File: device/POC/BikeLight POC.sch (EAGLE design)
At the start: 3 parts

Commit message: - added SD card with level shifter, FRAM module
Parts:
- added C1, C2, C3, C4, C5, C6: 0.1μF, rcl:C-EUC0805
- added IC3: FM25W256-SOIC, FM25W256 FERAM:FM25W256-SOIC
- added IC4: MICROSD_SPI_MODE, Molex SD-47309 SD Card Slot:MICROSD_SPI_MODE
- added IC5: (no value), TXB0106 - Logic Level Translator:TXB0106
- added R1, R3, R4, R5: 10k, rcl:R-EU_R0805
- added R2: 120, rcl:R-EU_R0805
- added X1, X2: 22-23-2021, con-molex:22-23-2021
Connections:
- removed net N$4: IC2.SI
- removed net N$5: IC2.SCK
- removed net N$6: IC2.!CS!
- removed net N$8: IC2.TXCAN
- removed net N$9: IC2.RXCAN
- removed net SPI_SS: U$1.D10
- new net 3V3: C4.1, C5.1, IC4.VCC, IC5.VCCA, R4.2
- new net 5V0: C1.1, C2.1, C3.1, C6.1, IC1.VCC, IC2.VDD, IC3.!HOLD!, IC3.!WP!, IC3.VCC, IC5.VCCB, R1.1, R3.2
- new net CANH: IC1.CANH, R2.2, X1-1.S
- new net CANL: IC1.CANL, R2.1, X1-2.S
- new net OE: IC5.OE, R5.2, U$1.D7
- new net RXCAN: IC1.RXD, IC2.RXCAN
- new net SD_CARD_DETECT: IC5.B6, U$1.D6
- new net SD_CARD_DETECT_3V3: IC4.CARD_DETECT, IC5.A6
- new net SPI_MISO_3V3: IC4.DO, IC5.A2
- new net SPI_MOSI_3V3: IC4.DI, IC5.A4
- new net SPI_SCK_3V3: IC4.CLK, IC5.A3
- new net SPI_SS_FRAM: IC3.!CS!, R3.1, U$1.D9
- new net SPI_SS_MCP2515: IC2.!CS!, R1.2, U$1.D10
- new net SPI_SS_SD-CARD: IC5.B5, U$1.D8
- new net SPI_SS_SD-CARD_3V3: IC4.CS, IC5.A5, R4.1
- new net STBY: IC1.STBY, U$1.D5
- new net TXCAN: IC1.TXD, IC2.TXCAN
- net GND: now also C1.2, C2.2, C3.2, C4.2, C5.2, C6.2, IC1.GND, IC2.GND, IC3.GND, IC4.GND1, IC4.GND2, IC4.GND3, IC4.GND4, IC5.GND, R5.1
- net N$3: now also IC2.OSC1; no longer IC2.SO
- net SPI_MISO: now also IC2.SO, IC3.SO, IC5.B2
- net SPI_MOSI: now also IC2.SI, IC3.SI, IC5.B4
- net SPI_SCK: now also IC2.SCK, IC3.SCK, IC5.B3
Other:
- moved on the sheet: IC1, IC2

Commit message: - added few passives to SD card, FRAM, logic level shifter, can hardware
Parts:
- added R6: 120, rcl:R-EU_R0805
- BRD1: value ARDUINOUNO -> (none)
- IC1: device MCP2561-2 - High-Speed CAN Transceiver:MCP2561-2 -> MCP2515-I-ML - Standalonce CAN Controller with SPI Interface:MCP2515-I-ML
- IC2: value (none) -> MICROSD_SPI_MODE; device MCP2515-I-ML - Standalonce CAN Controller with SPI Interface:MCP2515-I-ML -> Molex SD-47309 SD Card Slot:MICROSD_SPI_MODE
- IC4: value MICROSD_SPI_MODE -> (none); device Molex SD-47309 SD Card Slot:MICROSD_SPI_MODE -> MCP2561-2 - High-Speed CAN Transceiver:MCP2561-2
- R2: value 120 -> 10k
- renumbered U$1 to BRD1
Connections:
- net 3V3: now also C3.1, IC2.VCC, R3.2; no longer C4.1, IC4.VCC, R4.2
- net 5V0: now also C4.1, IC1.VDD, IC4.VCC, R2.2, R4.1; no longer C3.1, IC1.VCC, IC2.VDD, R3.2
- net CANH: now also IC4.CANH, R6.2, X2-1.S; no longer IC1.CANH, R2.2, X1-1.S
- net CANL: now also IC4.CANL, R6.1, X2-2.S; no longer IC1.CANL, R2.1, X1-2.S
- net GND: now also IC2.GND1, IC2.GND2, IC2.GND3, IC2.GND4, IC4.GND; no longer IC2.GND, IC4.GND1, IC4.GND2, IC4.GND3, IC4.GND4
- net N$3: now also IC1.OSC1; no longer IC2.OSC1
- net N$7: now also IC1.!INT!; no longer IC2.!INT!
- net RXCAN: now also IC1.RXCAN, IC4.RXD; no longer IC1.RXD, IC2.RXCAN
- net SD_CARD_DETECT_3V3: now also IC2.CARD_DETECT; no longer IC4.CARD_DETECT
- net SPI_MISO: now also IC1.SO; no longer IC2.SO
- net SPI_MISO_3V3: now also IC2.DO; no longer IC4.DO
- net SPI_MOSI: now also IC1.SI; no longer IC2.SI
- net SPI_MOSI_3V3: now also IC2.DI; no longer IC4.DI
- net SPI_SCK: now also IC1.SCK; no longer IC2.SCK
- net SPI_SCK_3V3: now also IC2.CLK; no longer IC4.CLK
- net SPI_SS_FRAM: now also R2.1; no longer R3.1
- net SPI_SS_MCP2515: now also IC1.!CS!; no longer IC2.!CS!
- net SPI_SS_SD-CARD_3V3: now also IC2.CS, R3.1; no longer IC4.CS, R4.1
- net STBY: now also IC4.STBY, R4.2; no longer IC1.STBY
- net TXCAN: now also IC1.TXCAN, IC4.TXD; no longer IC1.TXD, IC2.TXCAN
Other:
- moved on the sheet: C2, C3, C4, R2, R3, R4, X1-1, X1-2, X2-1, X2-2

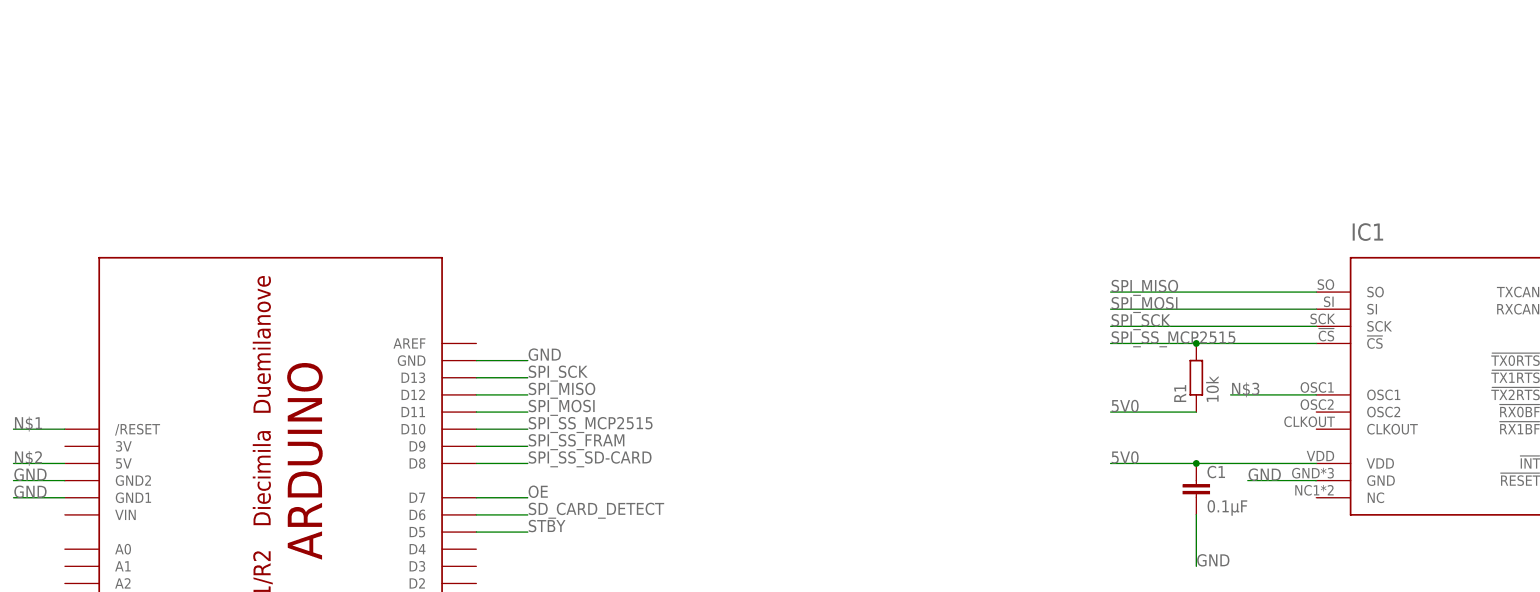
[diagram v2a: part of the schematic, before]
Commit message: - added 8mhz oscillator to mcp2515
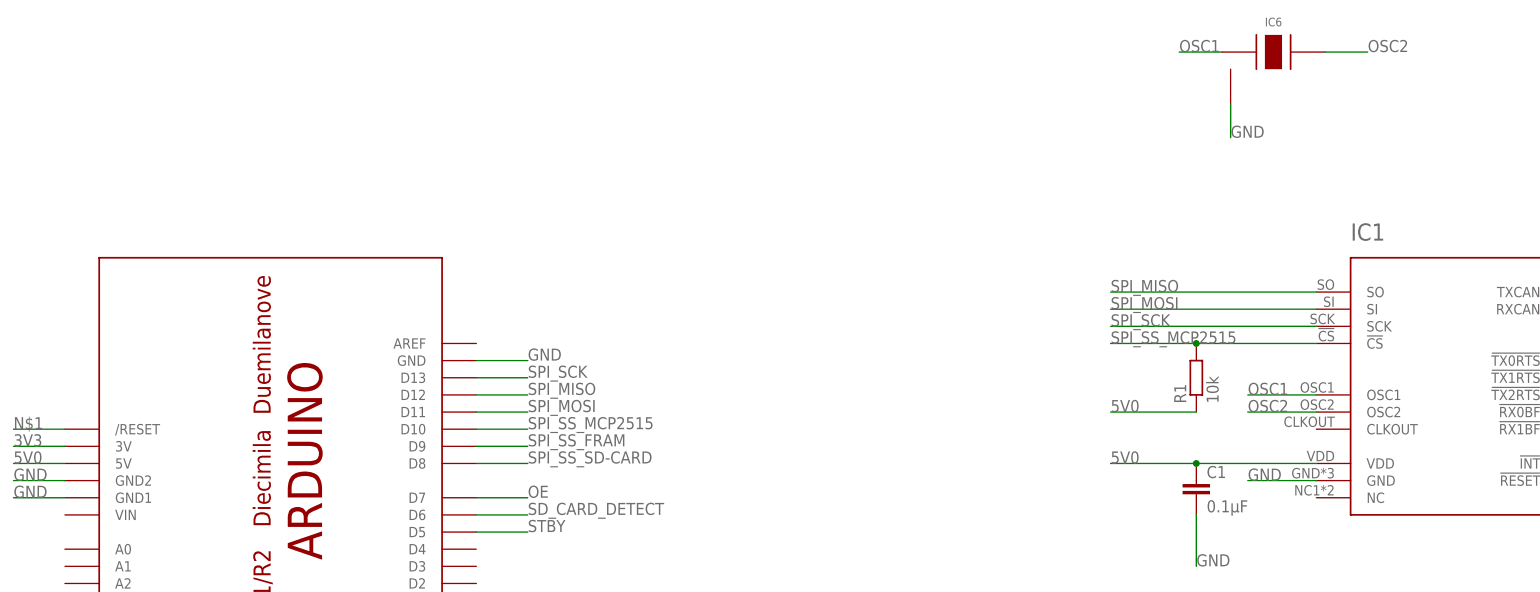
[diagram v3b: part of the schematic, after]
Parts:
- added IC6: (no value), PRQV8.00CR1510Y00L - 8MHz resonator:PRQV
- BRD1: value (none) -> BikeLight POC
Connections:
- removed net N$2: BRD1.5V
- removed net N$3: IC1.OSC1
- new net OSC1: IC1.OSC1, IC6.XTAL1
- new net OSC2: IC1.OSC2, IC6.XTAL2
- net 3V3: now also BRD1.3V
- net 5V0: now also BRD1.5V
- net GND: now also IC6.GND
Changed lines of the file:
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@@
 </classes>
 <parts>
-<part name="BRD1" library="adafruit" library_urn="urn:adsk.eagle:library:420" deviceset="ARDUINO" device="UNO"/>
+<part name="BRD1" library="adafruit" library_urn="urn:adsk.eagle:library:420" deviceset="ARDUINO" device="UNO" value="BikeLight POC"/>
 <part name="IC4" library="MCP2561-2 - High-Speed CAN Transceiver" deviceset="MCP2561-2" device=""/>
 <part name="IC1" library="MCP2515-I-ML - Standalonce CAN Controller with SPI Interface" deviceset="MCP2515-I-ML" device=""/>
@@
 <part name="R5" library="rcl" library_urn="urn:adsk.eagle:library:334" deviceset="R-EU_" device="R0805" package3d_urn="urn:adsk.eagle:package:23553/2" value="10k"/>
 <part name="R4" library="rcl" library_urn="urn:adsk.eagle:library:334" deviceset="R-EU_" device="R0805" package3d_urn="urn:adsk.eagle:package:23553/2" value="10k"/>
+<part name="IC6" library="PRQV8.00CR1510Y00L - 8MHz resonator" deviceset="PRQV" device=""/>
 </parts>
 <sheets>
@@
 <instance part="R5" gate="G$1" x="345.44" y="-99.06"/>
 <instance part="R4" gate="G$1" x="322.58" y="30.48" rot="R90"/>
+<instance part="IC6" gate="G$1" x="187.96" y="86.36"/>
 </instances>
 <busses>
@@
 <wire x1="10.16" y1="30.48" x2="2.54" y2="30.48" width="0.1524" layer="91"/>
 <label x="2.54" y="30.48" size="1.778" layer="95"/>
-</segment>
-</net>
-<net name="N$2" class="0">
-<segment>
-<pinref part="BRD1" gate="G$1" pin="5V"/>
-<wire x1="10.16" y1="25.4" x2="2.54" y2="25.4" width="0.1524" layer="91"/>
-<label x="2.54" y="25.4" size="1.778" layer="95"/>
 </segment>
 </net>
@@
 <label x="335.28" y="-99.06" size="1.778" layer="95"/>
 </segment>
+<segment>
+<pinref part="IC6" gate="G$1" pin="GND"/>
+<wire x1="182.88" y1="78.74" x2="182.88" y2="73.66" width="0.1524" layer="91"/>
+<label x="182.88" y="73.66" size="1.778" layer="95"/>
+</segment>
 </net>
 <net name="SPI_SCK" class="0">
@@
 <label x="322.58" y="20.32" size="1.778" layer="95"/>
 </segment>
+<segment>
+<pinref part="BRD1" gate="G$1" pin="5V"/>
+<wire x1="10.16" y1="25.4" x2="2.54" y2="25.4" width="0.1524" layer="91"/>
+<label x="2.54" y="25.4" size="1.778" layer="95"/>
+</segment>
 </net>
 <net name="STBY" class="0">
@@
 </segment>
 </net>
-<net name="N$3" class="0">
+<net name="OSC1" class="0">
 <segment>
 <pinref part="IC1" gate="G$1" pin="OSC1"/>
-<wire x1="195.58" y1="35.56" x2="182.88" y2="35.56" width="0.1524" layer="91"/>
-<label x="182.88" y="35.56" size="1.778" layer="95"/>
+<wire x1="195.58" y1="35.56" x2="185.42" y2="35.56" width="0.1524" layer="91"/>
+<label x="185.42" y="35.56" size="1.778" layer="95"/>
+</segment>
+<segment>
+<pinref part="IC6" gate="G$1" pin="XTAL1"/>
+<wire x1="181.61" y1="86.36" x2="175.26" y2="86.36" width="0.1524" layer="91"/>
+<label x="175.26" y="86.36" size="1.778" layer="95"/>
 </segment>
 </net>
@@
 <junction x="320.04" y="-114.3"/>
 </segment>
+<segment>
+<pinref part="BRD1" gate="G$1" pin="3V"/>
+<wire x1="10.16" y1="27.94" x2="2.54" y2="27.94" width="0.1524" layer="91"/>
+<label x="2.54" y="27.94" size="1.778" layer="95"/>
+</segment>
 </net>
 <net name="SPI_SS_SD-CARD_3V3" class="0">
@@
 </segment>
 </net>
+<net name="OSC2" class="0">
+<segment>
+<pinref part="IC1" gate="G$1" pin="OSC2"/>
+<wire x1="195.58" y1="33.02" x2="185.42" y2="33.02" width="0.1524" layer="91"/>
+<label x="185.42" y="33.02" size="1.778" layer="95"/>
+</segment>
+<segment>
+<pinref part="IC6" gate="G$1" pin="XTAL2"/>
+<wire x1="196.85" y1="86.36" x2="203.2" y2="86.36" width="0.1524" layer="91"/>
+<label x="203.2" y="86.36" size="1.778" layer="95"/>
+</segment>
+</net>
 </nets>
 </sheet>
 </sheets>
+<errors>
+</errors>
 </schematic>
 </drawing>

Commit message: - named arduino-uno compatible pins P0.XX - added ADXL345
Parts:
- added C7: 0.1μF, rcl:C-EUC0805
- added IC7: ADXL345, ADXL345 Accelerometer:ADXL345
- added IC8: (no value), 74HCT1G32GW - OR Gate:74HCT1G32GW-DC
- added R7: 10k, rcl:R-EU_R0805
- IC1: value (none) -> MCP2515-I-ML
- IC4: value (none) -> MCP2561-2
- IC5: value (none) -> TXB0106
- IC6: value (none) -> PRQV8.00CR1510Y00L
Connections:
- net N$7 renamed MCP2515_INT
- new net ADXL345_INT1_INTERRUPT_PIN: IC7.INT1
- new net N$2: IC7.SDA, IC8.Y
- new net P0.00-: BRD1.AREF
- new net P0.01-: BRD1.A0
- new net P0.02-: BRD1.A1
- new net P0.03-: BRD1.A2
- new net P0.04-: BRD1.A3
- new net P0.05-: BRD1.A4
- new net P0.06-: BRD1.A5
- new net P0.12-: BRD1.D0
- new net P0.13-: BRD1.D1
- new net P0.14-: BRD1.D2
- new net P0.15-MCP2515_INT: BRD1.D3
- new net P0.16-STBY: BRD1.D4
- new net P0.17-SD_CARD_DETECT: BRD1.D5
- new net P0.18-OE: BRD1.D6
- new net P0.19-SPI_SS_ADXL345_PIN: BRD1.D7
- new net P0.20-SPI_SS_SD-CARD: BRD1.D8
- new net P0.23-SPI_SS_FRAM: BRD1.D9
- new net P0.24-SPI_SS_MCP2515: BRD1.D10
- new net P0.25-SPI_MOSI: BRD1.D11
- new net P0.28-SPI_MISO: BRD1.D12
- new net P0.29-SPI_SCK: BRD1.D13
- new net SPI_MOSI_PIN: IC8.B
- new net SPI_SS_ADXL345_PIN: IC7.!CS!, IC8.A, R7.2
- net 5V0: now also C7.2, IC7.VDDIO, IC7.VS, R7.1
- net GND: now also C7.1, IC7.GND$1, IC7.GND$2, IC7.GND$3, IC8.GND
- net OE: no longer BRD1.D7
- net SD_CARD_DETECT: no longer BRD1.D6
- net SPI_MISO: now also IC7.SDO; no longer BRD1.D12
- net SPI_MOSI: no longer BRD1.D11
- net SPI_SCK: now also IC7.SCL; no longer BRD1.D13
- net SPI_SS_FRAM: no longer BRD1.D9
- net SPI_SS_MCP2515: no longer BRD1.D10
- net SPI_SS_SD-CARD: no longer BRD1.D8
- net STBY: no longer BRD1.D5

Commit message: - added MCP1802 LDO.lbr and datasheet - incorporated LDOs (3V3 and 5V0) into schematic - redeployed brd from scratch
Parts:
- added C10, C11, C8, C9: 4.7μF, rcl:C-EUC0805
- added IC10: MCP1802T-5002I/OT, MCP1802 LDO:MCP1802
- added IC9: MCP1802T-3302I/OT, MCP1802 LDO:MCP1802
- added R8: 100k, rcl:R-EU_R0805
- added S1: SWS001, smd-special:SWS001
- IC8: value (none) -> 74HCT1G32
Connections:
- net N$2 renamed SDA
- removed net ADXL345_INT1_INTERRUPT_PIN: IC7.INT1
- removed net MCP2515_INT: IC1.!INT!
- removed net OE: IC5.OE, R5.2
- removed net P0.01-: BRD1.A0
- removed net P0.13-: BRD1.D1
- removed net SD_CARD_DETECT: IC5.B6
- removed net SPI_MISO: IC1.SO, IC3.SO, IC5.B2, IC7.SDO
- removed net SPI_MOSI: IC1.SI, IC3.SI, IC5.B4
- removed net SPI_MOSI_PIN: IC8.B
- removed net SPI_SCK: IC1.SCK, IC3.SCK, IC5.B3, IC7.SCL
- removed net SPI_SS_ADXL345_PIN: IC7.!CS!, IC8.A, R7.2
- removed net SPI_SS_FRAM: IC3.!CS!, R2.1
- removed net SPI_SS_MCP2515: IC1.!CS!, R1.2
- removed net SPI_SS_SD-CARD: IC5.B5
- removed net STBY: IC4.STBY, R4.2
- new net !SNDN!: IC10.!SHDN!, IC9.!SHDN!, R8.2, S1.1
- new net P0.01-VLIION: BRD1.A0, C10.1, C8.1, IC10.VIN, IC9.VIN, S1.2, X1-1.S
- new net P0.13-ADXL345_INT1_INTERRUPT_PIN: BRD1.D1, IC7.INT1
- net 3V3: now also C9.1, IC9.VOUT
- net 5V0: now also C11.1, IC10.VOUT, IC8.VCC
- net GND: now also C10.2, C11.2, C8.2, C9.2, IC10.GND, IC9.GND, R8.1, X1-2.S
- net P0.15-MCP2515_INT: now also IC1.!INT!
- net P0.16-STBY: now also IC4.STBY, R4.2
- net P0.17-SD_CARD_DETECT: now also IC5.B6
- net P0.18-OE: now also IC5.OE, R5.2
- net P0.19-SPI_SS_ADXL345_PIN: now also IC7.!CS!, IC8.A, R7.2
- net P0.20-SPI_SS_SD-CARD: now also IC5.B5
- net P0.23-SPI_SS_FRAM: now also IC3.!CS!, R2.1
- net P0.24-SPI_SS_MCP2515: now also IC1.!CS!, R1.2
- net P0.25-SPI_MOSI: now also IC1.SI, IC3.SI, IC5.B4, IC8.B
- net P0.28-SPI_MISO: now also IC1.SO, IC3.SO, IC5.B2, IC7.SDO
- net P0.29-SPI_SCK: now also IC1.SCK, IC3.SCK, IC5.B3, IC7.SCL
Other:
- note added: "3V3 LDO"
- note added: "5V0 LDO"
- note added: "CAN Bus Connector"
- note added: "CAN Bus Controller"
- note added: "CAN Bus Transciever"
- note added: "LDO enable switch"
- note added: "LiIon Battery Connector"
- note added: "OR gate"
- note added: "SD Card"
- note added: "SPI Accelerometer w. OR Gate"
- note added: "SPI FRAM module"
- note added: "SPI SD Card w. logic-level translation"
- note added: "accelerometer"
- note added: "logic level translator"
- note added: "nRF51 Development Kit shield"
- note added: "terminator"
- moved on the sheet: C1, C2, C3, C4, C5, C6, C7, IC1, IC2, IC3, IC4, IC5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

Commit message: - finshed layout - added LED to indicate power-on status - remapped most pins to better fit board layout - ERC/DRC report no errors
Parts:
- added LED1: LTST-C230KSKT, led:LEDCHIPLED_1206
- added R9: 10k, rcl:R-EU_R0805
- added TP1, TP2, TP3, TP4: PTR1PAD1-13Y, testpad:PTR1PAD1-13Y
- added TP5, TP6, TP7, TP9: TPPAD1-13, testpad:TPPAD1-13
- renumbered X1 to LI-ION, X2 to CAN
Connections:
- removed net P0.13-ADXL345_INT1_INTERRUPT_PIN: BRD1.D1, IC7.INT1
- removed net P0.14-: BRD1.D2
- removed net P0.15-MCP2515_INT: BRD1.D3, IC1.!INT!
- removed net P0.16-STBY: BRD1.D4, IC4.STBY, R4.2
- removed net P0.17-SD_CARD_DETECT: BRD1.D5, IC5.B6
- removed net P0.18-OE: BRD1.D6, IC5.OE, R5.2
- removed net P0.19-SPI_SS_ADXL345_PIN: BRD1.D7, IC7.!CS!, IC8.A, R7.2
- removed net P0.20-SPI_SS_SD-CARD: BRD1.D8, IC5.B5
- removed net P0.23-SPI_SS_FRAM: BRD1.D9, IC3.!CS!, R2.1
- removed net P0.24-SPI_SS_MCP2515: BRD1.D10, IC1.!CS!, R1.2
- removed net P0.25-SPI_MOSI: BRD1.D11, IC1.SI, IC3.SI, IC5.B4, IC8.B
- removed net P0.28-SPI_MISO: BRD1.D12, IC1.SO, IC3.SO, IC5.B2, IC7.SDO
- removed net P0.29-SPI_SCK: BRD1.D13, IC1.SCK, IC3.SCK, IC5.B3, IC7.SCL
- new net N$2: LED1.C, R9.1
- new net P0.13-: BRD1.D1
- new net P0.14-STBY: BRD1.D2, IC4.STBY, R4.2
- new net P0.15-SPI_MISO: BRD1.D3, IC1.SO, IC3.SO, IC5.B2, IC7.SDO, TP3.TP
- new net P0.16-SPI_MOSI: BRD1.D4, IC1.SI, IC3.SI, IC5.B4, IC8.B, TP2.TP
- new net P0.17-SPI_SCK: BRD1.D5, IC1.SCK, IC3.SCK, IC5.B3, IC7.SCL, TP4.TP
- new net P0.18-SPI_SS_MCP2515: BRD1.D6, IC1.!CS!, R1.2, TP7.TP
- new net P0.19-MCP2515_INT: BRD1.D7, IC1.!INT!
- new net P0.20-ADXL345_INT1_INTERRUPT_PIN: BRD1.D8, IC7.INT1
- new net P0.23-SPI_SS_ADXL345_PIN: BRD1.D9, IC7.!CS!, IC8.A, R7.2, TP5.TP
- new net P0.24-SPI_SS_FRAM: BRD1.D10, IC3.!CS!, R2.1, TP6.TP
- new net P0.25-SPI_SS_SD-CARD: BRD1.D11, IC5.B5, TP9.TP
- new net P0.28-SD_CARD_DETECT: BRD1.D12, IC5.B6
- new net P0.29-OE: BRD1.D13, IC5.OE, R5.2
- net !SNDN!: now also LED1.A
- net CANH: now also CAN-2.S; no longer CAN-1.S
- net CANL: now also CAN-1.S; no longer CAN-2.S
- net GND: now also R9.2, TP1.TP
